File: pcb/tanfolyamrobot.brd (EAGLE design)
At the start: 81.3 x 58.7 mm, 78 parts, among them IC1 STM32F10XRXT6, IC2 7805, IC4 FT232RL, IC5 LD117AS33TR, M1 DRV8833, Q2 BSS123, Q3 BSS123, Q4 BSS123, X2 PWR, X6 KUSBVX-BS1N

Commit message: small schematic fixes #1
added notes
added component values/types
made RESET and BOOT0 circuit nicer
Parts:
- C10: value (none) -> 22u
- C11: value (none) -> 330n
- C12: value (none) -> 100n
- C13: value 1u -> 100n
- C14: value 2u2 -> 10u
- C16: value (none) -> 68u
- C17: value 22n? -> 22n
- C5, C6: value ? -> 15p
- D7: value (none) -> BAS85
- Q1: value (none) -> 16MHz
- R20, R21: value (none) -> 10K
- R22, R23: value (none) -> 20K
- R24, R25: value (none) -> 4K7

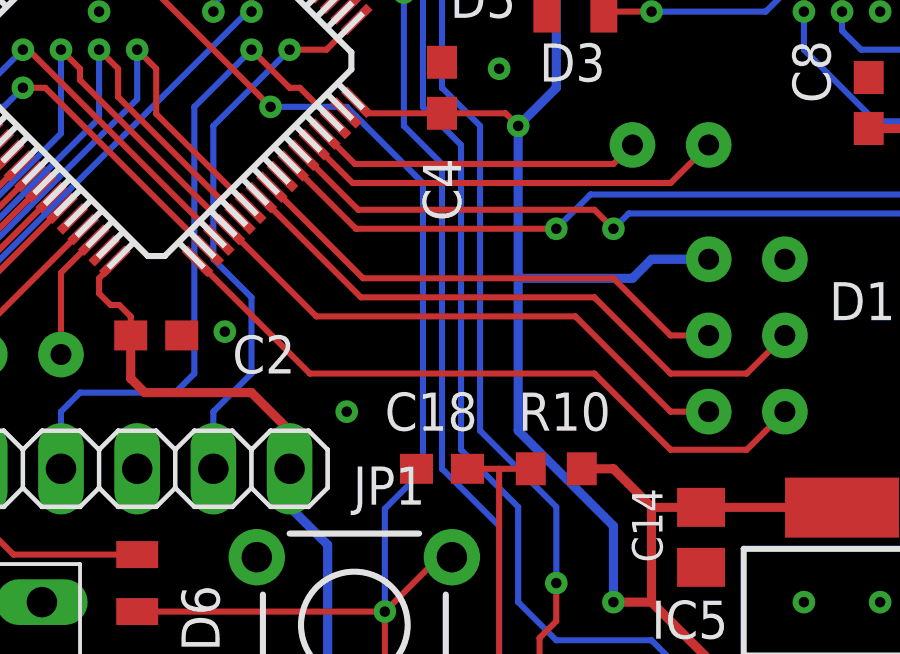
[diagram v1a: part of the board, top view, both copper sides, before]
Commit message: added 100n cap to NRST (#1)
and also added ESP reset description
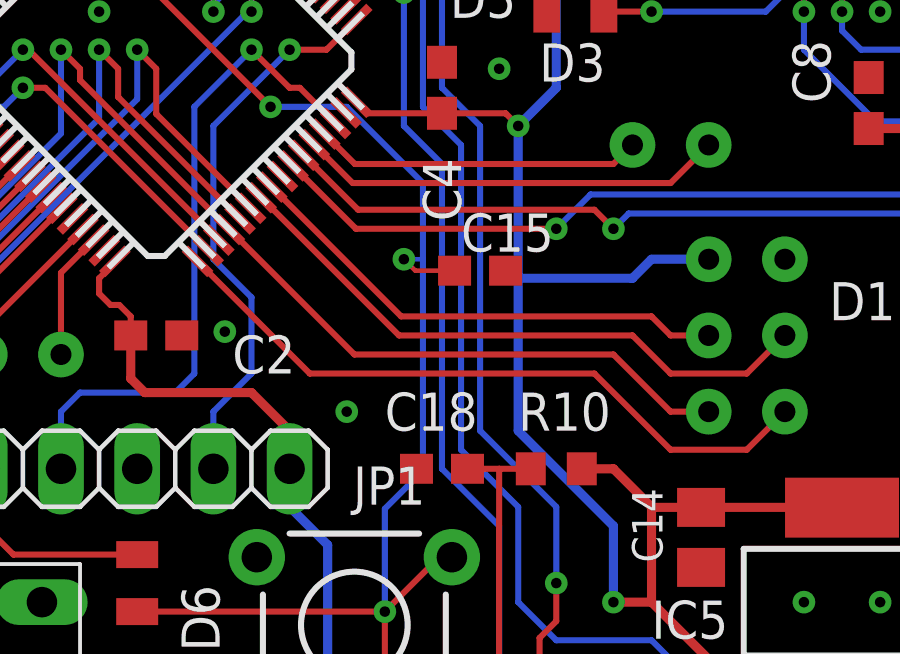
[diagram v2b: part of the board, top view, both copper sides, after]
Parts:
- added C15: 100n, rcl:C0603
- R29: value (none) -> 4K7
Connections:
- net GND: now also C15.2
- net RSTN: now also C15.1
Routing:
- net RSTN: track 80.0 -> 82.5 mm, vias 4 -> 5
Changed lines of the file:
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@@
 <attribute name="VALUE" x="67.16" y="17.684" size="1.27" layer="27" rot="R270"/>
 </element>
-<element name="R29" library="rcl" library_urn="urn:adsk.eagle:library:334" package="R0603" package3d_urn="urn:adsk.eagle:package:23555/3" value="" x="50.165" y="42.545" smashed="yes" rot="R180">
+<element name="R29" library="rcl" library_urn="urn:adsk.eagle:library:334" package="R0603" package3d_urn="urn:adsk.eagle:package:23555/3" value="4K7" x="50.165" y="42.545" smashed="yes" rot="R180">
 <attribute name="NAME" x="48.26" y="44.45" size="1.27" layer="25" rot="R180"/>
 <attribute name="POPULARITY" value="70" x="50.165" y="42.545" size="1.778" layer="27" rot="R180" display="off"/>
@@
 <attribute name="SPICEPREFIX" value="R" x="14.605" y="31.115" size="1.778" layer="27" rot="R270" display="off"/>
 <attribute name="VALUE" x="12.7" y="31.75" size="1.27" layer="27" rot="R270"/>
+</element>
+<element name="C15" library="rcl" library_urn="urn:adsk.eagle:library:334" package="C0603" package3d_urn="urn:adsk.eagle:package:23616/2" value="100n" x="43.18" y="26.289" smashed="yes">
+<attribute name="NAME" x="42.545" y="26.924" size="1.27" layer="25"/>
+<attribute name="POPULARITY" value="73" x="43.18" y="26.289" size="1.778" layer="27" display="off"/>
+<attribute name="SPICEPREFIX" value="C" x="43.18" y="26.289" size="1.778" layer="27" display="off"/>
+<attribute name="VALUE" x="42.545" y="24.384" size="1.27" layer="27"/>
 </element>
 </elements>
@@
 <contactref element="JP16" pad="3"/>
 <contactref element="Q4" pad="2"/>
+<contactref element="C15" pad="2"/>
 </signal>
 <signal name="+3V3">
@@
 <wire x1="49.315" y1="38.735" x2="49.315" y2="40.54" width="0.2032" layer="1"/>
 <wire x1="49.315" y1="40.54" x2="49.215" y2="40.64" width="0.2032" layer="1"/>
-<wire x1="41.275" y1="29.21" x2="41.275" y2="19.624" width="0.2032" layer="16"/>
+<wire x1="41.275" y1="29.21" x2="41.275" y2="26.67" width="0.2032" layer="16"/>
+<wire x1="41.275" y1="26.67" x2="41.275" y2="19.624" width="0.2032" layer="16"/>
 <wire x1="41.275" y1="19.624" x2="40.005" y2="18.354" width="0.2032" layer="16"/>
 <wire x1="40.005" y1="18.354" x2="40.005" y2="14.925" width="0.2032" layer="16"/>
@@
 <wire x1="47.879" y1="41.275" x2="47.879" y2="42.037" width="0.2032" layer="1"/>
 <wire x1="48.514" y1="40.64" x2="47.879" y2="41.275" width="0.2032" layer="1"/>
+<contactref element="C15" pad="1"/>
+<wire x1="42.33" y1="26.289" x2="41.021" y2="26.289" width="0.1524" layer="1"/>
+<wire x1="41.021" y1="26.289" x2="40.64" y2="26.67" width="0.1524" layer="1"/>
+<via x="40.64" y="26.67" extent="1-16" drill="0.35"/>
+<wire x1="40.64" y1="26.67" x2="41.275" y2="26.67" width="0.1524" layer="16"/>
 </signal>
 <signal name="N$6">
@@
 <contactref element="IC1" pad="39"/>
 <via x="53.34" y="24.13" extent="1-16" drill="0.7" diameter="1.524"/>
-<wire x1="35.885178125" y1="28.722184375" x2="39.2073625" y2="25.4" width="0.2032" layer="1"/>
-<wire x1="39.2073625" y1="25.4" x2="46.99" y2="25.4" width="0.2032" layer="1"/>
+<wire x1="35.885178125" y1="28.722184375" x2="40.4773625" y2="24.13" width="0.2032" layer="1"/>
+<wire x1="40.4773625" y1="24.13" x2="48.26" y2="24.13" width="0.2032" layer="1"/>
 <wire x1="52.07" y1="22.86" x2="53.34" y2="24.13" width="0.2032" layer="1"/>
-<wire x1="46.99" y1="25.4" x2="49.53" y2="22.86" width="0.2032" layer="1"/>
+<wire x1="48.26" y1="24.13" x2="49.53" y2="22.86" width="0.2032" layer="1"/>
 <wire x1="49.53" y1="22.86" x2="52.07" y2="22.86" width="0.2032" layer="1"/>
 </signal>
@@
 <contactref element="IC1" pad="40"/>
 <via x="50.8" y="24.13" extent="1-16" drill="0.7" diameter="1.524"/>
-<wire x1="36.23873125" y1="29.0757375" x2="39.27946875" y2="26.035" width="0.2032" layer="1"/>
-<wire x1="39.27946875" y1="26.035" x2="47.625" y2="26.035" width="0.2032" layer="1"/>
+<wire x1="36.23873125" y1="29.0757375" x2="40.54946875" y2="24.765" width="0.2032" layer="1"/>
+<wire x1="40.54946875" y1="24.765" x2="48.895" y2="24.765" width="0.2032" layer="1"/>
 <wire x1="50.8" y1="24.13" x2="49.53" y2="24.13" width="0.2032" layer="1"/>
-<wire x1="49.53" y1="24.13" x2="47.625" y2="26.035" width="0.2032" layer="1"/>
+<wire x1="49.53" y1="24.13" x2="48.895" y2="24.765" width="0.2032" layer="1"/>
 </signal>
 <signal name="PA4">
@@
 <contactref element="IC1" pad="36"/>
 <via x="50.8" y="21.59" extent="1-16" drill="0.7" diameter="1.524"/>
-<wire x1="34.824515625" y1="27.661525" x2="37.721040625" y2="24.765" width="0.2032" layer="1"/>
-<wire x1="37.721040625" y1="24.765" x2="46.355" y2="24.765" width="0.2032" layer="1"/>
+<wire x1="34.824515625" y1="27.661525" x2="38.991040625" y2="23.495" width="0.2032" layer="1"/>
+<wire x1="38.991040625" y1="23.495" x2="47.625" y2="23.495" width="0.2032" layer="1"/>
 <wire x1="50.8" y1="21.59" x2="49.53" y2="21.59" width="0.2032" layer="1"/>
-<wire x1="49.53" y1="21.59" x2="46.355" y2="24.765" width="0.2032" layer="1"/>
+<wire x1="49.53" y1="21.59" x2="47.625" y2="23.495" width="0.2032" layer="1"/>
 <wire x1="34.824515625" y1="27.661525" x2="29.845" y2="32.641040625" width="0.2032" layer="1"/>
 <wire x1="29.845" y1="33.02" x2="29.845" y2="32.641040625" width="0.2032" layer="1"/>

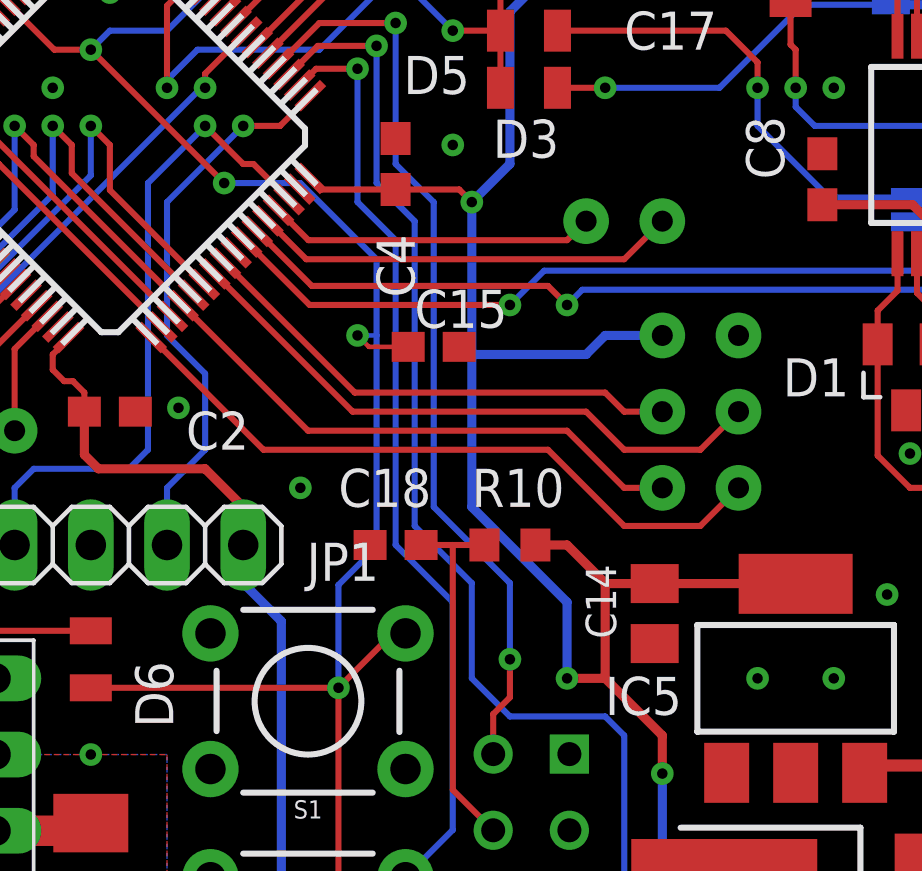
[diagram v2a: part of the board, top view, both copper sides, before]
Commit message: fixed unused pin header connections (#1)
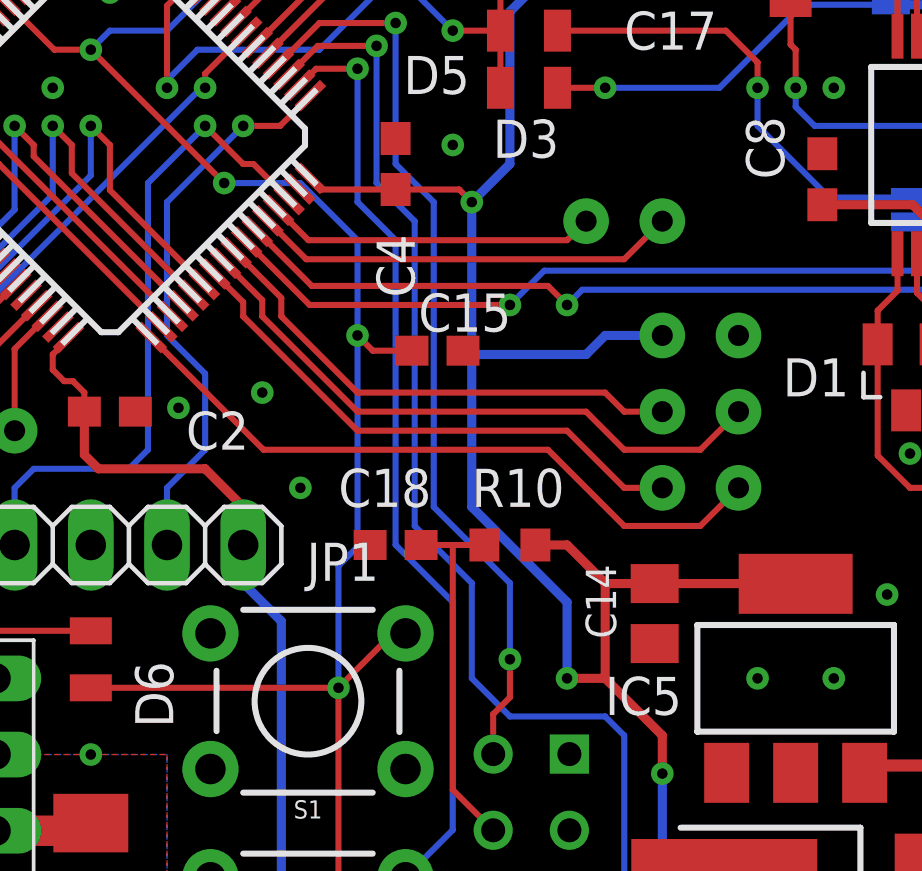
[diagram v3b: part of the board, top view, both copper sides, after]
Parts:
- moved C15 0.18 mm to (43.3, 26.2)
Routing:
- net SERVO: track 51.6 -> 33.1 mm, vias 3 -> 2
- net PA8: track 0.00 -> 16.8 mm, vias 0 -> 1
- net PC9: track 16.6 -> 20.5 mm
- net PC8: track 20.4 -> 18.1 mm
- net RSTN: track 82.5 -> 81.5 mm
- net GND: vias 54 -> 55
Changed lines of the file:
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@@
 <attribute name="VALUE" x="12.7" y="31.75" size="1.27" layer="27" rot="R270"/>
 </element>
-<element name="C15" library="rcl" library_urn="urn:adsk.eagle:library:334" package="C0603" package3d_urn="urn:adsk.eagle:package:23616/2" value="100n" x="43.18" y="26.289" smashed="yes">
-<attribute name="NAME" x="42.545" y="26.924" size="1.27" layer="25"/>
-<attribute name="POPULARITY" value="73" x="43.18" y="26.289" size="1.778" layer="27" display="off"/>
-<attribute name="SPICEPREFIX" value="C" x="43.18" y="26.289" size="1.778" layer="27" display="off"/>
-<attribute name="VALUE" x="42.545" y="24.384" size="1.27" layer="27"/>
+<element name="C15" library="rcl" library_urn="urn:adsk.eagle:library:334" package="C0603" package3d_urn="urn:adsk.eagle:package:23616/2" value="100n" x="43.307" y="26.162" smashed="yes">
+<attribute name="NAME" x="42.672" y="26.797" size="1.27" layer="25"/>
+<attribute name="POPULARITY" value="73" x="43.307" y="26.162" size="1.778" layer="27" display="off"/>
+<attribute name="SPICEPREFIX" value="C" x="43.307" y="26.162" size="1.778" layer="27" display="off"/>
+<attribute name="VALUE" x="42.672" y="24.257" size="1.27" layer="27"/>
 </element>
 </elements>
@@
 <contactref element="Q4" pad="2"/>
 <contactref element="C15" pad="2"/>
+<via x="37.465" y="24.765" extent="1-16" drill="0.35"/>
 </signal>
 <signal name="+3V3">
@@
 <wire x1="47.879" y1="42.037" x2="48.387" y2="42.545" width="0.2032" layer="1"/>
 <wire x1="48.387" y1="42.545" x2="49.315" y2="42.545" width="0.2032" layer="1"/>
-<wire x1="41.275" y1="29.21" x2="38.735" y2="31.75" width="0.2032" layer="16"/>
+<wire x1="40.64" y1="29.845" x2="38.735" y2="31.75" width="0.2032" layer="16"/>
 <wire x1="36.195" y1="31.75" x2="38.735" y2="31.75" width="0.2032" layer="16"/>
 <via x="36.195" y="31.75" extent="1-16" drill="0.35"/>
@@
 <wire x1="49.315" y1="38.735" x2="49.315" y2="40.54" width="0.2032" layer="1"/>
 <wire x1="49.315" y1="40.54" x2="49.215" y2="40.64" width="0.2032" layer="1"/>
-<wire x1="41.275" y1="29.21" x2="41.275" y2="26.67" width="0.2032" layer="16"/>
-<wire x1="41.275" y1="26.67" x2="41.275" y2="19.624" width="0.2032" layer="16"/>
-<wire x1="41.275" y1="19.624" x2="40.005" y2="18.354" width="0.2032" layer="16"/>
-<wire x1="40.005" y1="18.354" x2="40.005" y2="14.925" width="0.2032" layer="16"/>
+<wire x1="40.64" y1="29.845" x2="40.64" y2="26.67" width="0.2032" layer="16"/>
+<wire x1="40.64" y1="26.67" x2="40.64" y2="19.624" width="0.2032" layer="16"/>
+<wire x1="40.64" y1="19.624" x2="40.005" y2="18.989" width="0.2032" layer="16"/>
+<wire x1="40.005" y1="18.989" x2="40.005" y2="14.925" width="0.2032" layer="16"/>
 <contactref element="U$1" pad="RST"/>
 <wire x1="45.1625" y1="7.635" x2="43.8775" y2="6.35" width="0.2032" layer="1"/>
@@
 <wire x1="48.514" y1="40.64" x2="47.879" y2="41.275" width="0.2032" layer="1"/>
 <contactref element="C15" pad="1"/>
-<wire x1="42.33" y1="26.289" x2="41.021" y2="26.289" width="0.1524" layer="1"/>
-<wire x1="41.021" y1="26.289" x2="40.64" y2="26.67" width="0.1524" layer="1"/>
+<wire x1="42.457" y1="26.162" x2="41.148" y2="26.162" width="0.2032" layer="1"/>
+<wire x1="41.148" y1="26.162" x2="40.64" y2="26.67" width="0.2032" layer="1"/>
 <via x="40.64" y="26.67" extent="1-16" drill="0.35"/>
-<wire x1="40.64" y1="26.67" x2="41.275" y2="26.67" width="0.1524" layer="16"/>
 </signal>
 <signal name="N$6">
@@
 <signal name="PC8">
 <contactref element="IC1" pad="39"/>
-<via x="53.34" y="24.13" extent="1-16" drill="0.7" diameter="1.524"/>
-<wire x1="35.885178125" y1="28.722184375" x2="40.4773625" y2="24.13" width="0.2032" layer="1"/>
-<wire x1="40.4773625" y1="24.13" x2="48.26" y2="24.13" width="0.2032" layer="1"/>
-<wire x1="52.07" y1="22.86" x2="53.34" y2="24.13" width="0.2032" layer="1"/>
-<wire x1="48.26" y1="24.13" x2="49.53" y2="22.86" width="0.2032" layer="1"/>
-<wire x1="49.53" y1="22.86" x2="52.07" y2="22.86" width="0.2032" layer="1"/>
+<via x="50.8" y="21.59" extent="1-16" drill="0.7" diameter="1.524"/>
+<wire x1="35.885178125" y1="28.722184375" x2="36.83" y2="27.7773625" width="0.2032" layer="1"/>
+<wire x1="36.83" y1="27.305" x2="40.64" y2="23.495" width="0.2032" layer="1"/>
+<wire x1="49.53" y1="21.59" x2="50.8" y2="21.59" width="0.2032" layer="1"/>
+<wire x1="36.83" y1="27.7773625" x2="36.83" y2="27.305" width="0.2032" layer="1"/>
+<wire x1="40.64" y1="23.495" x2="47.625" y2="23.495" width="0.2032" layer="1"/>
+<wire x1="47.625" y1="23.495" x2="49.53" y2="21.59" width="0.2032" layer="1"/>
 </signal>
 <signal name="PC9">
 <contactref element="IC1" pad="40"/>
-<via x="50.8" y="24.13" extent="1-16" drill="0.7" diameter="1.524"/>
-<wire x1="36.23873125" y1="29.0757375" x2="40.54946875" y2="24.765" width="0.2032" layer="1"/>
-<wire x1="40.54946875" y1="24.765" x2="48.895" y2="24.765" width="0.2032" layer="1"/>
-<wire x1="50.8" y1="24.13" x2="49.53" y2="24.13" width="0.2032" layer="1"/>
-<wire x1="49.53" y1="24.13" x2="48.895" y2="24.765" width="0.2032" layer="1"/>
+<via x="53.34" y="24.13" extent="1-16" drill="0.7" diameter="1.524"/>
+<wire x1="53.34" y1="24.13" x2="52.07" y2="22.86" width="0.2032" layer="1"/>
+<wire x1="37.465" y1="27.305" x2="40.64" y2="24.13" width="0.2032" layer="1"/>
+<wire x1="52.07" y1="22.86" x2="49.53" y2="22.86" width="0.2032" layer="1"/>
+<wire x1="49.53" y1="22.86" x2="48.26" y2="24.13" width="0.2032" layer="1"/>
+<wire x1="48.26" y1="24.13" x2="40.64" y2="24.13" width="0.2032" layer="1"/>
+<wire x1="36.23873125" y1="29.0757375" x2="37.465" y2="27.84946875" width="0.2032" layer="1"/>
+<wire x1="37.465" y1="27.84946875" x2="37.465" y2="27.305" width="0.2032" layer="1"/>
 </signal>
 <signal name="PA4">
@@
 <wire x1="26.035" y1="27.686" x2="10.414" y2="27.686" width="0.2032" layer="16"/>
 <contactref element="IC1" pad="36"/>
-<via x="50.8" y="21.59" extent="1-16" drill="0.7" diameter="1.524"/>
-<wire x1="34.824515625" y1="27.661525" x2="38.991040625" y2="23.495" width="0.2032" layer="1"/>
-<wire x1="38.991040625" y1="23.495" x2="47.625" y2="23.495" width="0.2032" layer="1"/>
-<wire x1="50.8" y1="21.59" x2="49.53" y2="21.59" width="0.2032" layer="1"/>
-<wire x1="49.53" y1="21.59" x2="47.625" y2="23.495" width="0.2032" layer="1"/>
 <wire x1="34.824515625" y1="27.661525" x2="29.845" y2="32.641040625" width="0.2032" layer="1"/>
 <wire x1="29.845" y1="33.02" x2="29.845" y2="32.641040625" width="0.2032" layer="1"/>
@@
 <signal name="PA8">
 <contactref element="IC1" pad="41"/>
+<via x="50.8" y="24.13" extent="1-16" drill="0.7" diameter="1.524"/>
+<wire x1="36.592284375" y1="29.429290625" x2="38.1" y2="27.921575" width="0.2032" layer="1"/>
+<wire x1="38.1" y1="27.921575" x2="38.1" y2="27.305" width="0.2032" layer="1"/>
+<wire x1="38.1" y1="27.305" x2="40.64" y2="24.765" width="0.2032" layer="1"/>
+<wire x1="48.895" y1="24.765" x2="49.53" y2="24.13" width="0.2032" layer="1"/>
+<wire x1="49.53" y1="24.13" x2="50.8" y2="24.13" width="0.2032" layer="1"/>
+<wire x1="40.64" y1="24.765" x2="48.895" y2="24.765" width="0.2032" layer="1"/>
 </signal>
 </signals>
